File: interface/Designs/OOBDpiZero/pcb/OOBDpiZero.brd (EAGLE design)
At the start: 73.5 x 42 mm, 133 parts, among them IC1 LM1117MPX-3.3, IC11 EEPROM24, IC3 DS3231, Q2 12MHz, U1 SN65HVD230(SO8), U2 SN65HVD230(SO8), U3 MAX98357, U4 SY6280, U5 MP1482

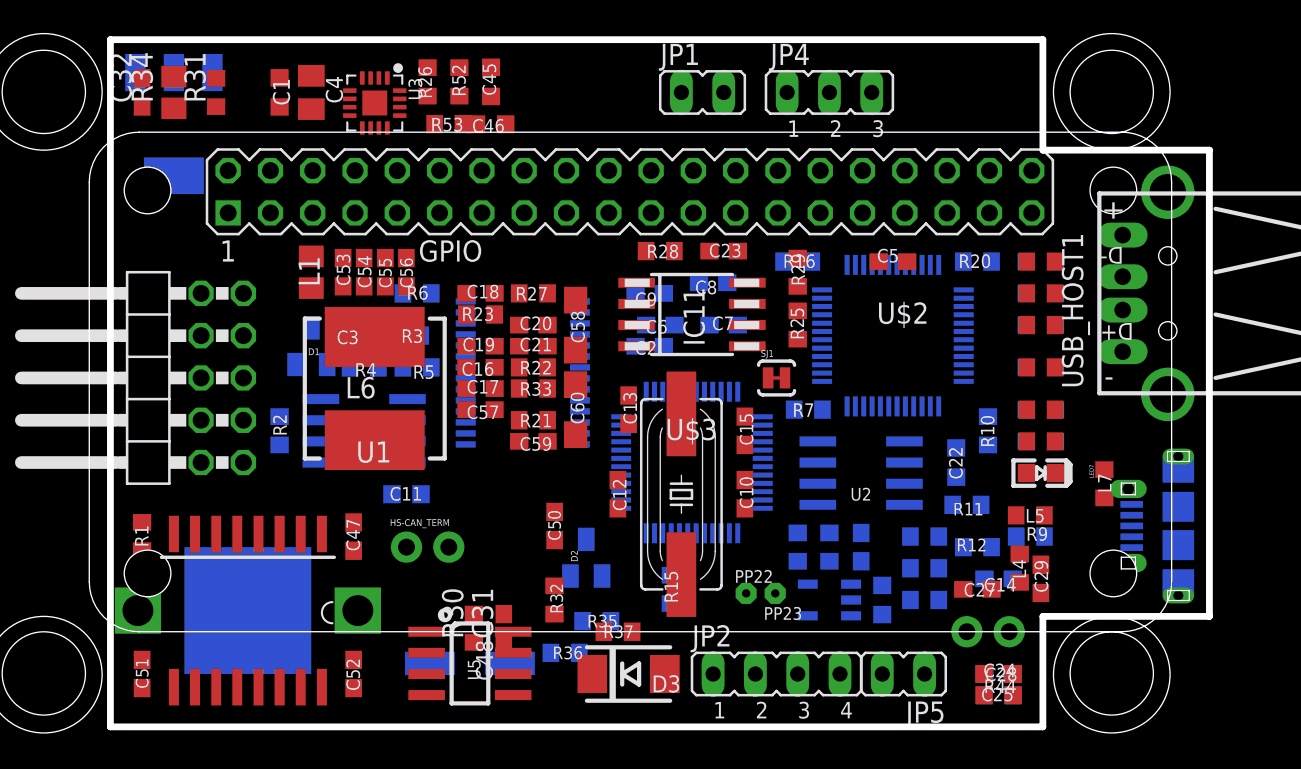
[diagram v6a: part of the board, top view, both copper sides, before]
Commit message: Automatic routed plus hand routed lines. Ongoing
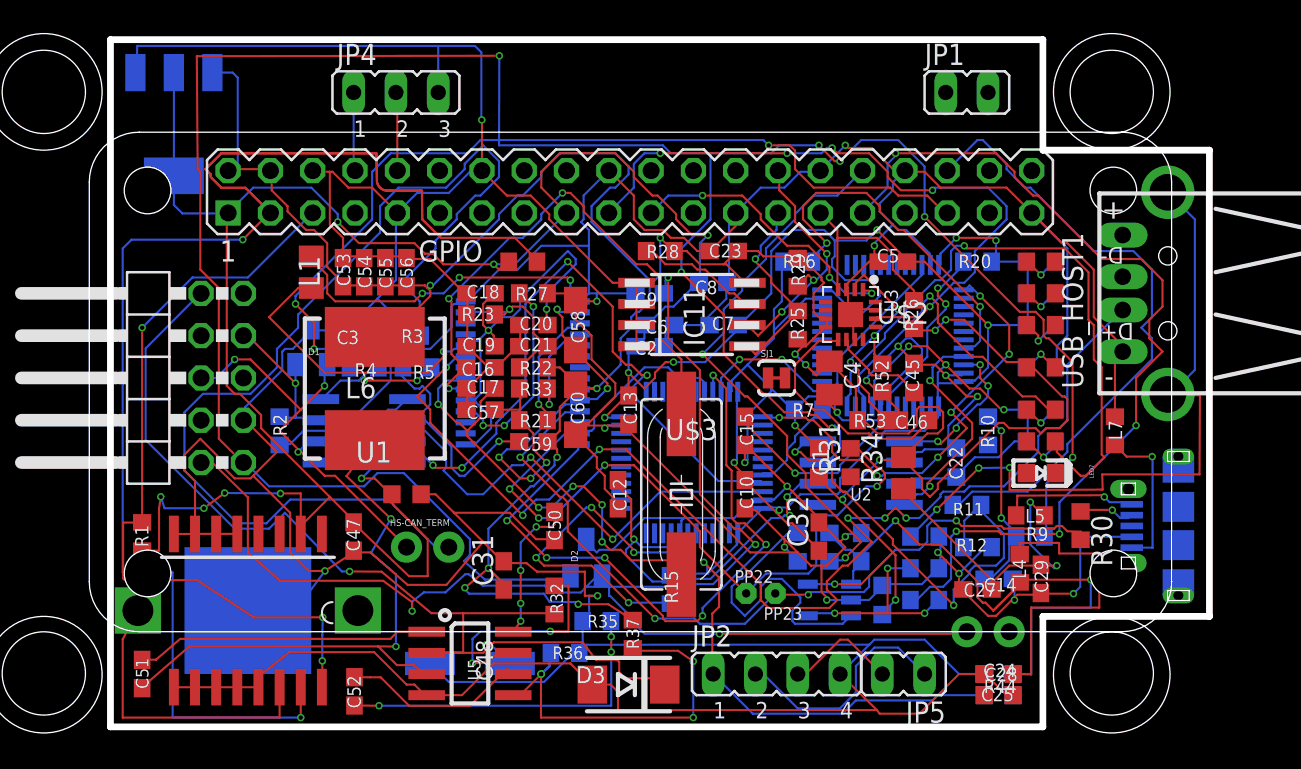
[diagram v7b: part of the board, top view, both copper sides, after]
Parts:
- moved R34 49.4 mm to (47.6, 14.6)
- moved C32 48.6 mm to (42.5, 10.8)
- moved R31 44.1 mm to (44.5, 15.2)
- moved C1 39.3 mm to (42.5, 15.2)
- moved R30 37.0 mm to (58.3, 11.5), turned to 270 degrees
- moved C4 35.5 mm to (43.2, 20.3)
- moved R26 32.4 mm to (48.3, 24.1)
- moved U3 31.3 mm to (44.5, 24.1)
- moved C45 31.0 mm to (48.3, 20.3)
- moved C46 31.0 mm to (48.3, 17.8)
- moved R52 31.0 mm to (46.4, 20.3)
- moved R53 31.0 mm to (45.7, 17.8)
- moved JP4 26.0 mm to (17.1, 37.5)
- moved JP1 15.9 mm to (51.4, 37.5)
- moved R6 6.63 mm to (24.8, 27.3), flipped to the top
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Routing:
- net GND: track 0.00 -> 578.7 mm, vias 0 -> 23
- net +3V3: track 0.00 -> 285.7 mm, vias 0 -> 22
- net +5V: track 0.00 -> 188.4 mm, vias 0 -> 15
- net MS-CAN_H: track 0.00 -> 154.3 mm, vias 0 -> 7
- net SDA: track 0.00 -> 104.0 mm, vias 0 -> 2
- net MS-CAN_L: track 0.00 -> 72.4 mm, vias 0 -> 4
- net USB2_DP: track 0.00 -> 70.9 mm, vias 0 -> 6
- net N$30: track 0.00 -> 64.5 mm
- net +12V: track 0.00 -> 62.7 mm, vias 0 -> 2
- net USB_CE: track 0.00 -> 54.4 mm, vias 0 -> 4
- net HS-CAN_RS: track 0.00 -> 53.7 mm, vias 0 -> 3
- net PP23: track 0.00 -> 48.0 mm, vias 0 -> 4
- net N$20: track 0.00 -> 47.9 mm, vias 0 -> 6
- net N$33: track 0.00 -> 46.3 mm, vias 0 -> 8
- net SCL: track 0.00 -> 46.2 mm, vias 0 -> 3
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
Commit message: Nur noch 14 Lines….
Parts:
- moved C29 0.38 mm to (55.9, 8.64)
- moved MS-CAN_TERM 0.38 mm to (51.1, 4.95)
- moved SJ1 0.33 mm to (39.7, 20.4), turned to 180 degrees
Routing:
- net N$48: track 8.36 -> 41.7 mm, vias 1 -> 2
- net SWCLK: track 34.1 -> 56.8 mm
- net USB1_EN: track 12.4 -> 22.3 mm
- net N$46: track 7.40 -> 16.0 mm
- net GND: track 578.7 -> 582.3 mm, vias 23 -> 24
- net N$80: track 27.5 -> 30.5 mm
- net +3V3: track 285.7 -> 288.1 mm, vias 22 -> 23
- net N$26: track 0.00 -> 1.74 mm
- net N$42: track 41.6 -> 40.9 mm
- net USB2_DP: track 70.9 -> 71.4 mm
